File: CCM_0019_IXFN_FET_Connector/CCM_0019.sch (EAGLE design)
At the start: 7 parts, among them X1 22-23-2021

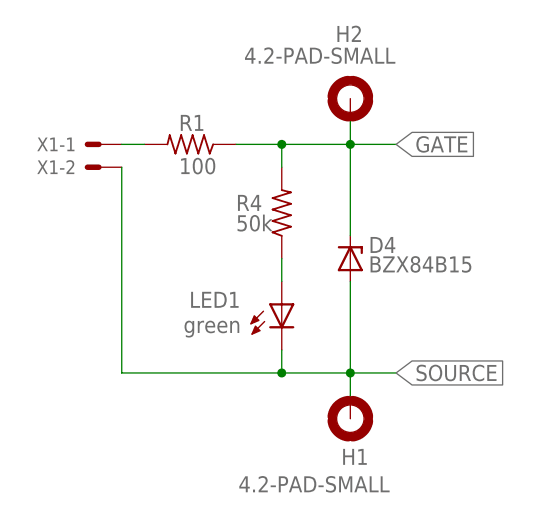
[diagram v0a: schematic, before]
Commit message: Updated designs for MOT coil control and H-bridge switching
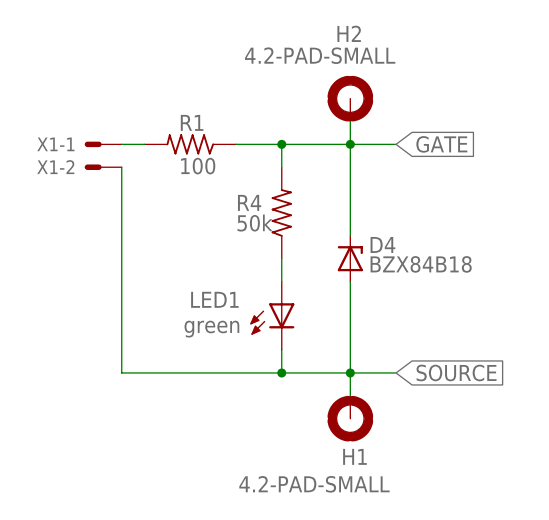
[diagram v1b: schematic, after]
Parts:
- D4: value BZX84B15 -> BZX84B18
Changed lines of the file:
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@@
 <?xml version="1.0" encoding="utf-8"?>
 <!DOCTYPE eagle SYSTEM "eagle.dtd">
-<eagle version="9.0.1">
+<eagle version="9.2.1">
 <drawing>
 <settings>
@@
 <parts>
 <part name="FRAME1" library="frames" library_urn="urn:adsk.eagle:library:229" deviceset="A4L-LOC" device=""/>
-<part name="D4" library="diode" library_urn="urn:adsk.eagle:library:210" deviceset="ZENER-DIODE" device="SOT23" package3d_urn="urn:adsk.eagle:package:43389@1/2" value="BZX84B15"/>
+<part name="D4" library="diode" library_urn="urn:adsk.eagle:library:210" deviceset="ZENER-DIODE" device="SOT23" package3d_urn="urn:adsk.eagle:package:43389@1/2" value="BZX84B18"/>
 <part name="R1" library="noah" deviceset="RESISTOR" device="0603" value="100"/>
 <part name="R4" library="noah" deviceset="RESISTOR" device="0603" value="50k"/>
@@
 </plain>
 <instances>
-<instance part="FRAME1" gate="G$1" x="0" y="0"/>
+<instance part="FRAME1" gate="G$1" x="0" y="0" smashed="yes">
+<attribute name="DRAWING_NAME" x="217.17" y="15.24" size="2.54" layer="94"/>
+<attribute name="LAST_DATE_TIME" x="217.17" y="10.16" size="2.286" layer="94"/>
+<attribute name="SHEET" x="230.505" y="5.08" size="2.54" layer="94"/>
+</instance>
 <instance part="D4" gate="G$1" x="73.66" y="40.64" smashed="yes" rot="R90">
 <attribute name="NAME" x="75.692" y="41.275" size="1.778" layer="95"/>
